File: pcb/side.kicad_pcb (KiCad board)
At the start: 2 copper layers, 97.8 x 81.2 mm, 46 parts, among them J1 R0, J10 R3, J2 C0, J3 R3, J4 C2, J5 Conn_01x12_Socket, J6 Conn_01x12_Socket, J7 C0, J8 R0, J9 C2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

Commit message: small updates
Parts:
- added H1: MountingHole, zzkeeb:Hole_M2, F.Cu at (120.0, 76.0)
- added H2: MountingHole, zzkeeb:Hole_M2, F.Cu at (101.0, 64.0)
- added H3: MountingHole, zzkeeb:Hole_M2, F.Cu at (151.0, 104.0)
- added H4: MountingHole, zzkeeb:Hole_M2, F.Cu at (82.0, 86.0)
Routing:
- net row0: track 151.0 -> 148.2 mm
- net Net-(D8-A): track 30.2 -> 29.3 mm
- net SW16_R3: track 86.9 -> 87.6 mm
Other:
- outline, holes or cut-outs redrawn
- board text added: "JLCJLCJLCJLC"
- board text added: "github.com/zzeneg/trio"

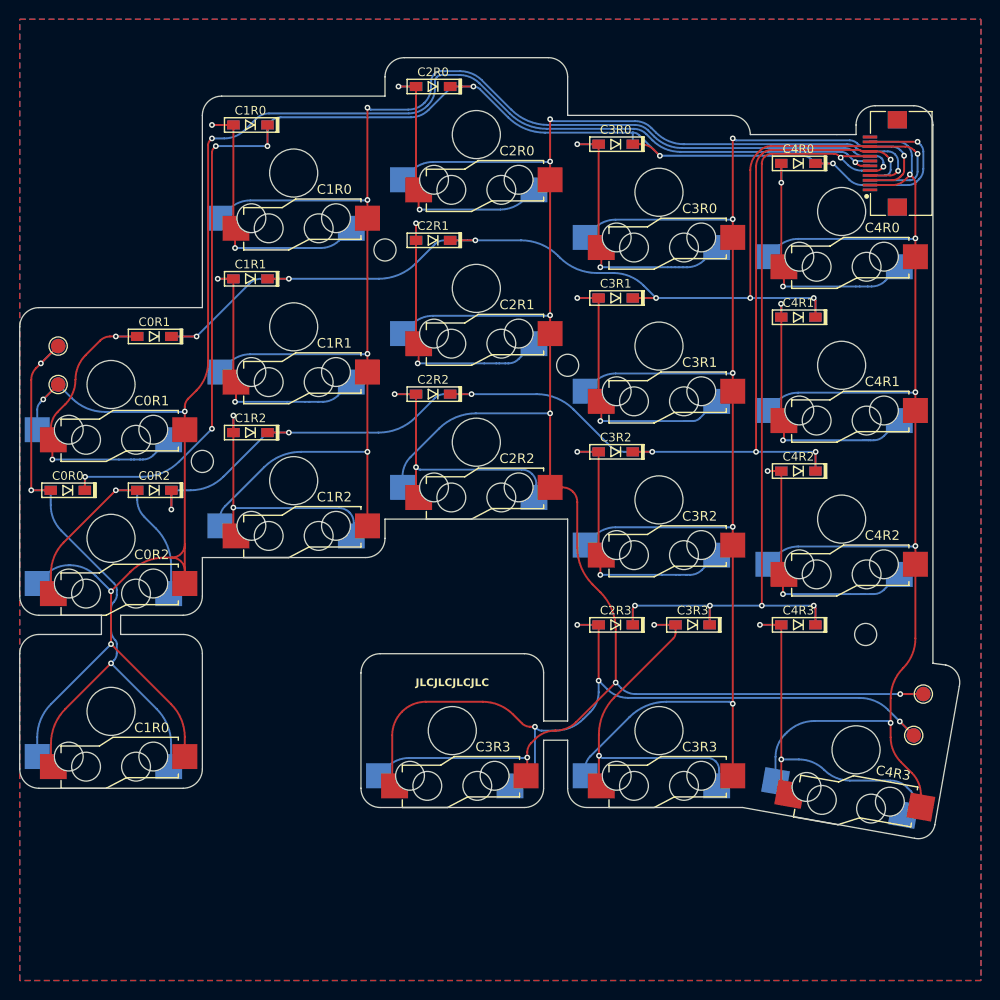
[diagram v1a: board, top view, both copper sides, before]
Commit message: jumpers for VIK GPIO, small side updates
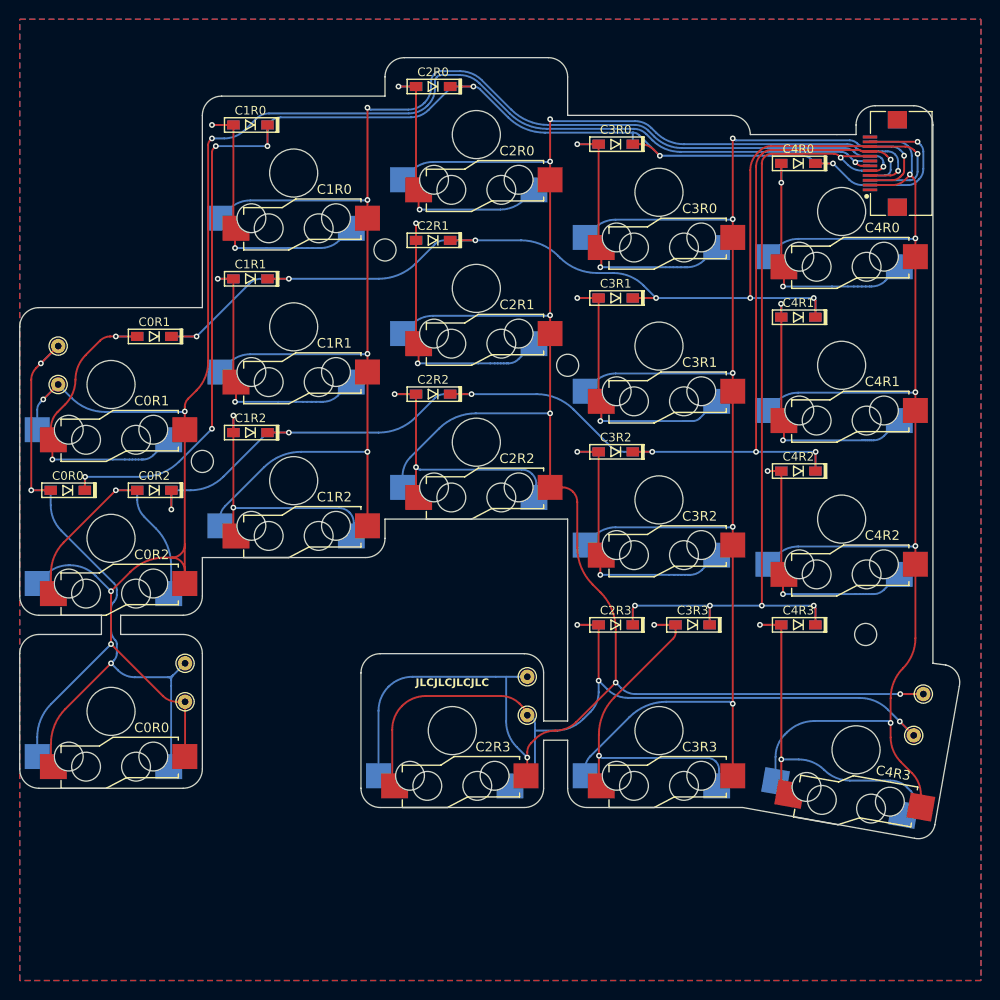
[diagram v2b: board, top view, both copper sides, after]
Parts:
- J1, J10, J2, J4: footprint TestPoint:TestPoint_Pad_D1.5mm -> TestPoint:TestPoint_THTPad_D1.5mm_Drill0.7mm
- J3, J7, J8, J9: footprint TestPoint:TestPoint_Pad_D1.5mm -> TestPoint:TestPoint_THTPad_D1.5mm_Drill0.7mm; moved to F.Cu
- moved J9 41.2 mm to (115.8, 108.4), turned to 0 degrees
- moved J10 40.3 mm to (115.8, 112.4)
- moved J2 35.5 mm to (80.2, 111.0)
- moved J8 35.5 mm to (80.2, 107.0), turned to 0 degrees
- turned J3 to 0 degrees
- turned J7 to 0 degrees
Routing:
- net col2: track 220.4 -> 237.6 mm
- net SW1_R0: track 70.1 -> 75.8 mm
- net SW16_R3: track 87.6 -> 88.8 mm, vias 4 -> 3
- net col0: track 201.3 -> 202.4 mm
